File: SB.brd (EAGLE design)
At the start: 78 x 34 mm, 48 parts, among them IC1 ATMEGA32U4NT-TQFP, IC2 HX711-SOP16L, J2 RJ12, J3 AUDIO-JACK-PJ321, J4 NO/NC, J5 USB-C-16P-16P, K1 HE721C-DIP, Q1 2N7002, Q2 2N7002, Q3 2N3906

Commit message: Routing for v2.0 release
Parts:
- removed J4: NO/NC, SuperHouse-Connectors:1X03-P
- added SW1: SWITCH-SPDT-4TABSSMT, SuperHouse-Switches:MK-12C02
- L1: device SuperHouse-DiscreteSemi:0603 -> SuperHouse-DiscreteSemi:L0603
- MOD1: value OLED-I2C-128X32-0.91 -> OLED-I2C-128X32-0.91-HEADER; device SuperHouse-Displays:OLED-128X32-0.91 -> SuperHouse-Displays:OLED-128X32-0.91-HEADER
- moved C9 48.3 mm to (18.0, 3.50)
- moved R10 48.3 mm to (15.0, 2.50)
- moved R9 48.3 mm to (15.0, 4.50)
- moved R13 47.5 mm to (19.0, 8.50)
- moved IC2 47.2 mm to (29.0, 6.00)
- moved C8 46.7 mm to (23.0, 5.50)
- moved Q3 46.6 mm to (22.0, 11.0)
- moved C10 45.6 mm to (17.0, 10.5)
- moved R14 45.3 mm to (21.0, 7.00)
- moved C12 43.2 mm to (29.0, 12.0)
- moved C11 41.2 mm to (17.0, 14.5), turned to 90 degrees
- moved L1 38.5 mm to (19.0, 12.5), turned to 270 degrees
- moved R7 10.3 mm to (71.5, 16.0)
- moved C1 5.10 mm to (38.0, 17.0)
- moved C2 5.10 mm to (38.0, 14.5)
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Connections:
- net A+: now also J2.3; no longer J2.4
- net A-: now also J2.4; no longer J2.3
- net GND: now also SW1.MNT@1, SW1.MNT@2, SW1.MNT@3, SW1.MNT@4
- net N$4: now also K1.14, SW1.3; no longer J4.3, K1.1
- net N$6: now also K1.1, SW1.1; no longer J4.1, K1.14
- net N$9: now also SW1.2; no longer J4.2
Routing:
- net N$4: track 7.05 -> 57.6 mm
- net N$9: track 41.8 -> 10.4 mm
- net N$2: track 2.12 -> 28.6 mm, vias 0 -> 1
- net N$6: track 12.4 -> 34.8 mm
- net A+: track 0.00 -> 17.3 mm
- net E+: track 0.00 -> 17.3 mm
- net 5V: track 71.3 -> 86.4 mm, vias 5 -> 6
- net RESET: track 21.5 -> 35.6 mm
- net N$14: track 0.00 -> 11.2 mm
- net N$15: track 0.00 -> 11.1 mm
- net N$16: track 0.00 -> 10.9 mm
- net A-: track 0.00 -> 8.47 mm
- net D4_A6: track 45.6 -> 37.3 mm, vias 1 -> 2
- net N$21: track 0.00 -> 7.77 mm
- net N$20: track 0.00 -> 5.18 mm
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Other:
- board text added: "A+"
- board text added: "A-"
- board text added: "E+"
- board text added: "E-"
- board text added: "H+"
- board text added: "H-"

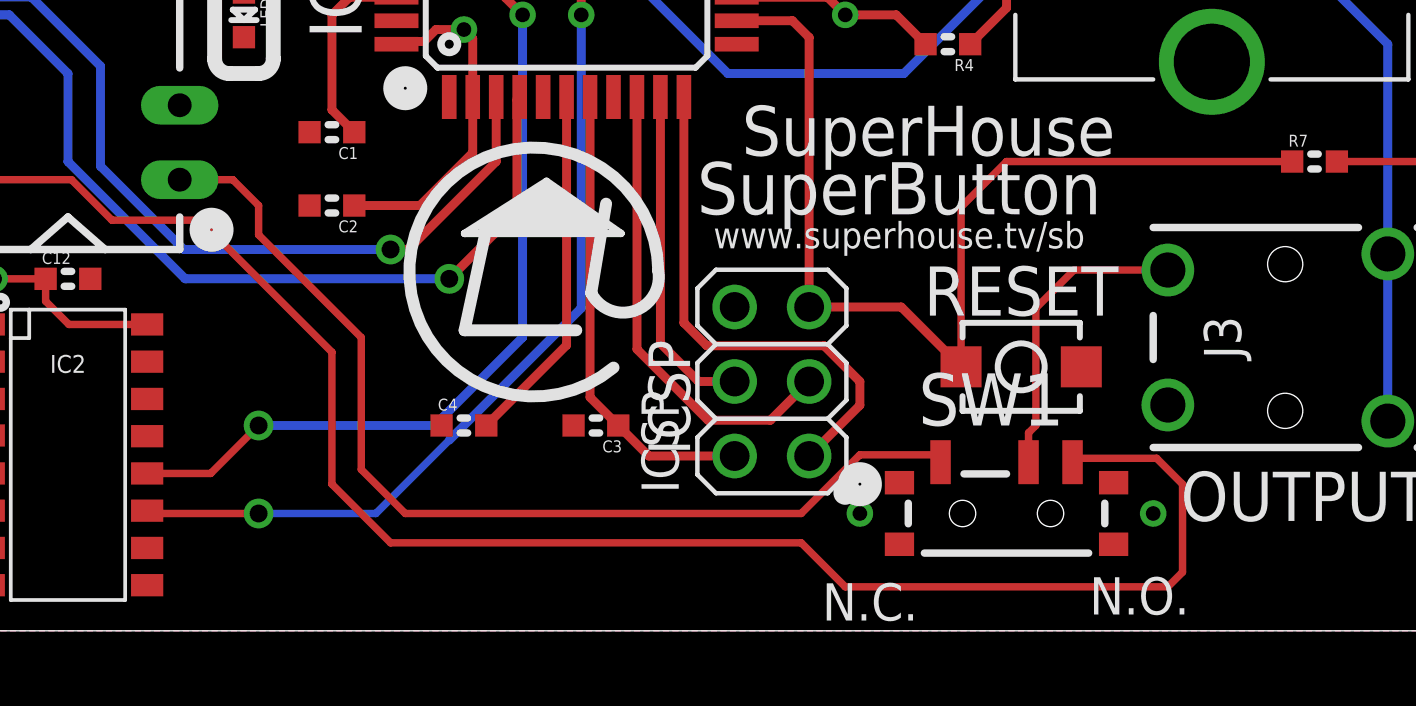
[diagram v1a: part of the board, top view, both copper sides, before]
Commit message: Synch with Fusion 360
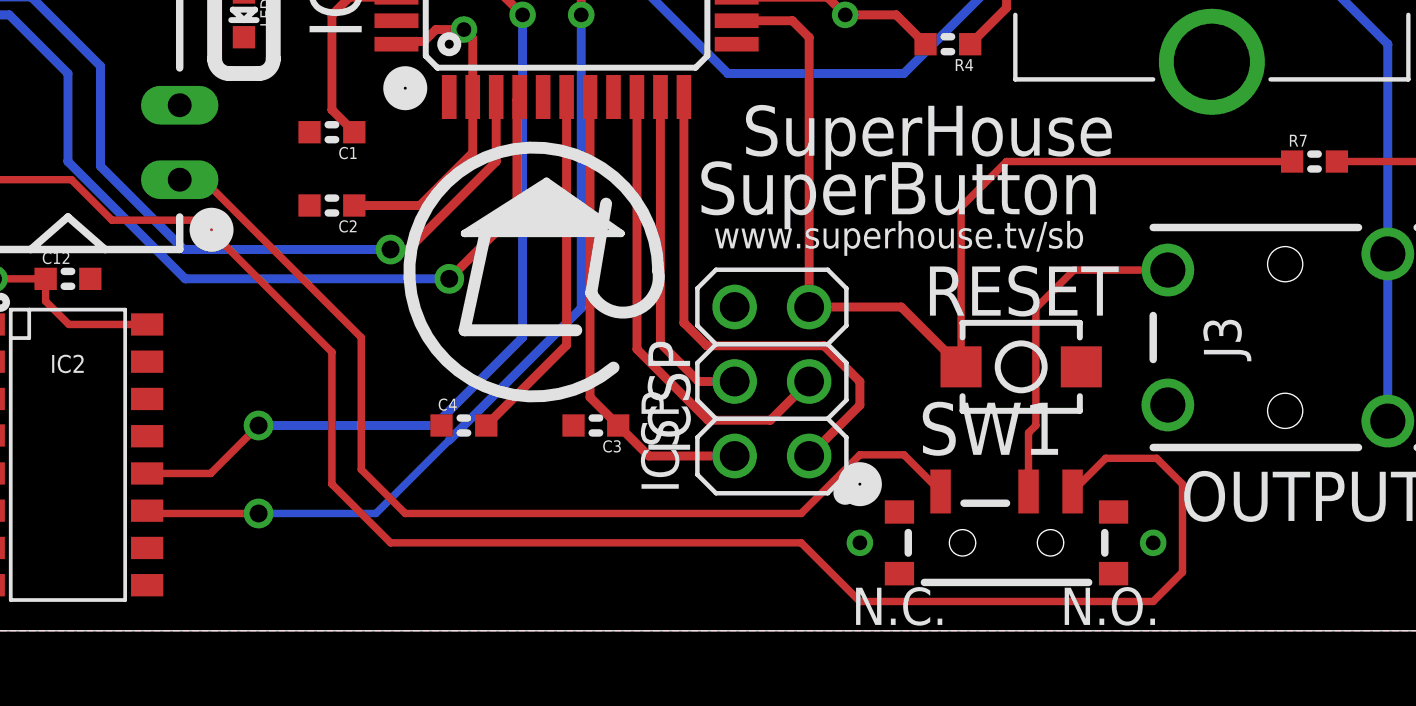
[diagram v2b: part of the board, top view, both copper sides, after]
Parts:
- R5, R6: value 4K7 -> 5k1
- moved SW1 1.00 mm to (61.0, 3.00)
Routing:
- net N$9: track 10.4 -> 11.4 mm
- net N$4: track 57.6 -> 58.4 mm
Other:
- board text added: "(C)2020 SuperHouse Automation P/L"
- board text removed: "(C)2019 SuperHouse Automation P/L"

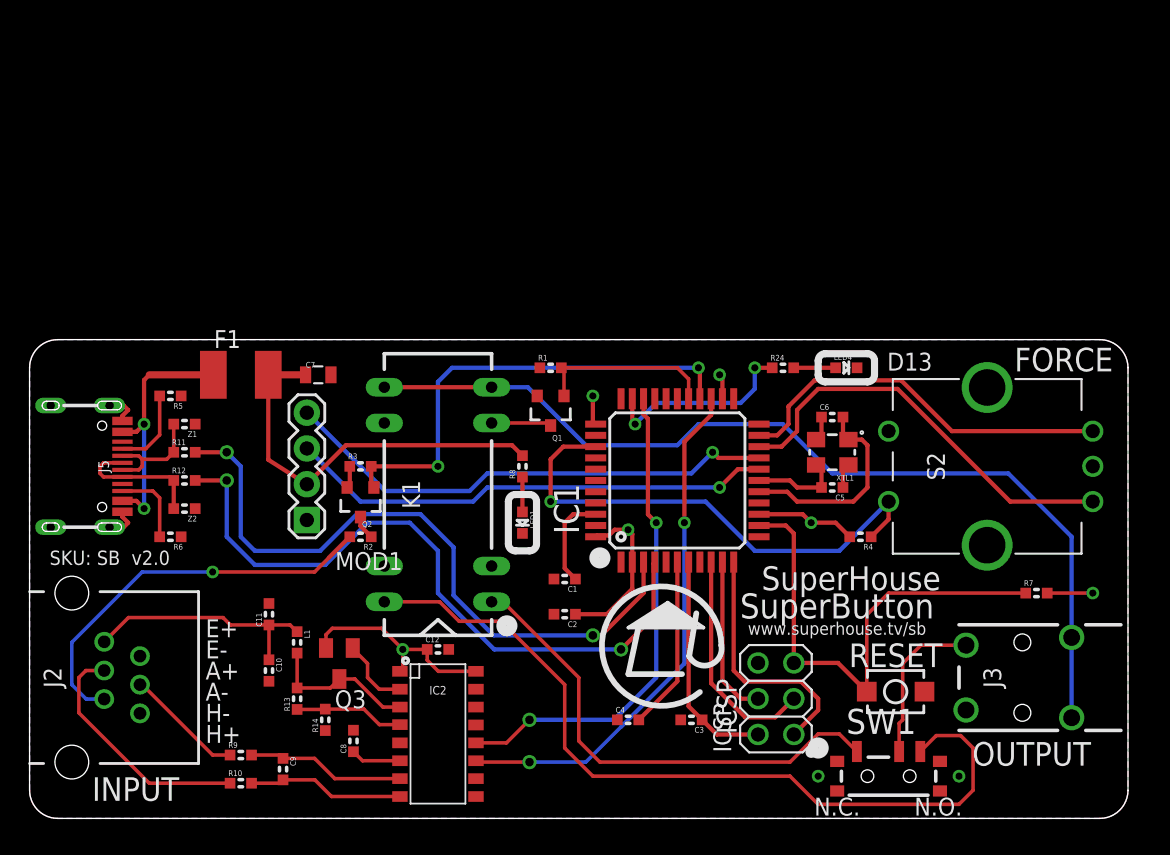
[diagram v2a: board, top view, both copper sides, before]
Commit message: Added mounting holes for v2.1 release
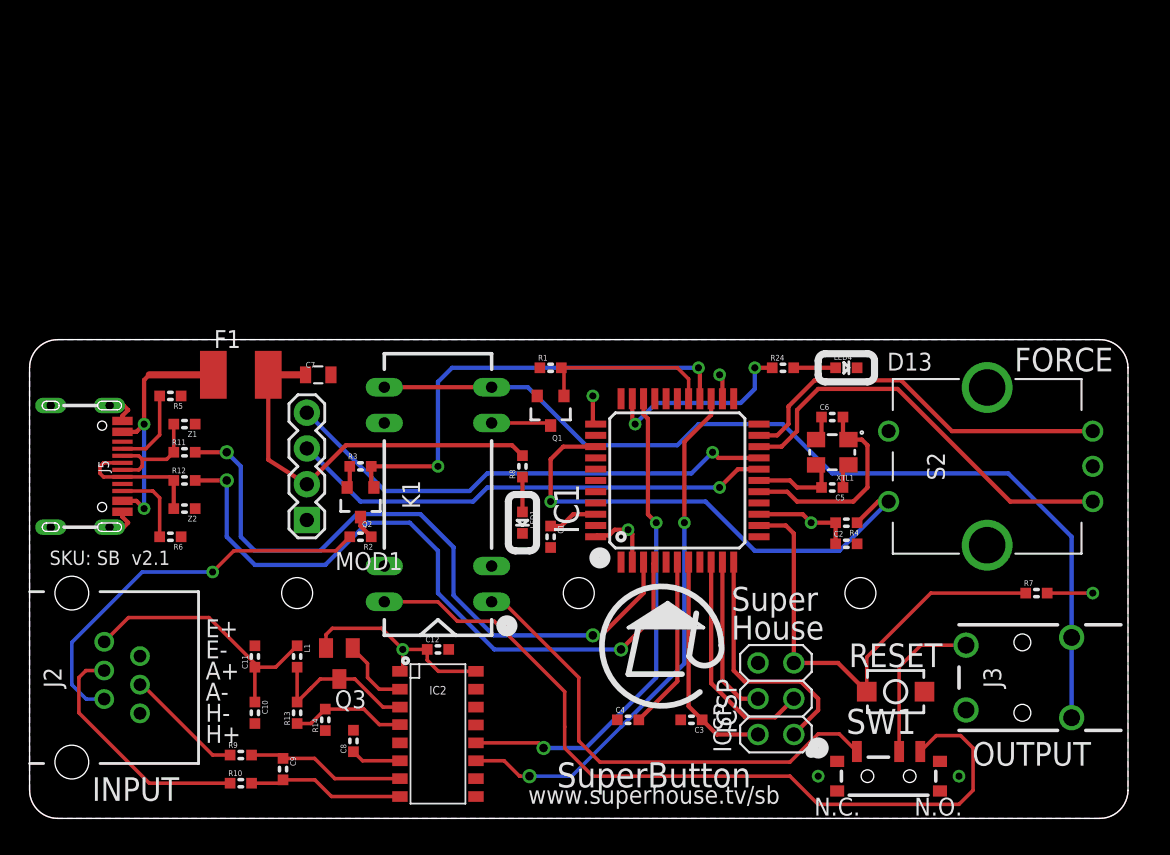
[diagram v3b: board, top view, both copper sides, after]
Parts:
- moved C2 20.6 mm to (58.0, 19.5), turned to 0 degrees
- moved C1 3.16 mm to (37.0, 20.0), turned to 270 degrees
- moved C10 3.16 mm to (16.0, 7.50)
- moved C11 3.16 mm to (16.0, 11.5)
- moved R4 1.41 mm to (58.0, 21.0)
- moved L1 1.00 mm to (19.0, 11.5)
- moved R13 1.00 mm to (19.0, 7.50)
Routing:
- net 5V: track 86.4 -> 79.8 mm
- net AREF: track 6.76 -> 3.55 mm
- net E+: track 17.3 -> 19.1 mm
- net RESET: track 35.6 -> 33.8 mm
- net D4_A6: track 37.3 -> 38.2 mm
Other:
- board text added: "SKU: SB v2.1"
- board text added: "Super House"
- board text removed: "SKU: SB v2.0"
- board text removed: "SuperHouse"

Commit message: Added Tare button and beep stretch switch, still for v2.1 release
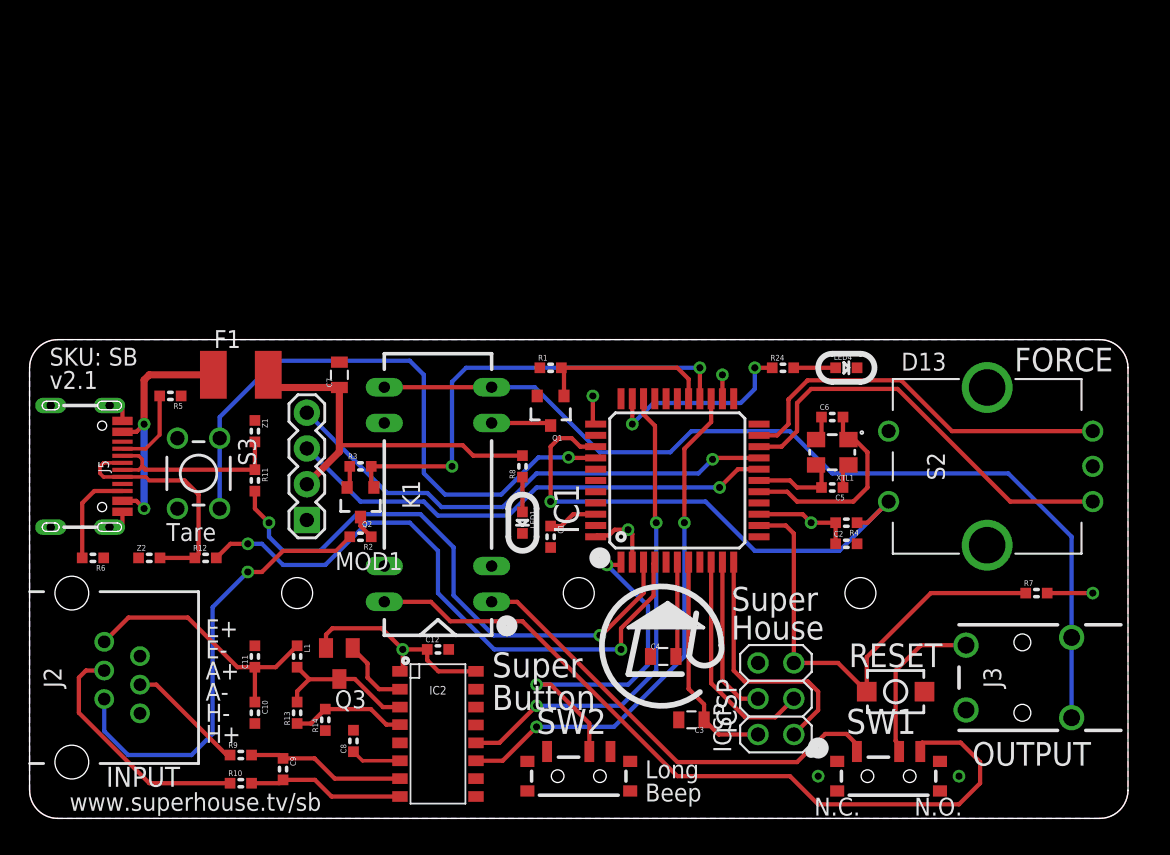
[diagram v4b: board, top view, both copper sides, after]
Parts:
- added S3: (no value), SuperHouse-Switches:TACTILE-PTH-4.5MM
- added SW2: SWITCH-SPDT-4TABSSMT, SuperHouse-Switches:MK-12C02
- C3, C4: device SuperHouse-DiscreteSemi:C0603 -> SuperHouse-DiscreteSemi:C0805
- moved R12 5.70 mm to (12.5, 18.5)
- moved R6 5.70 mm to (4.50, 18.5)
- moved R11 5.39 mm to (16.0, 24.0), turned to 270 degrees
- moved C4 5.15 mm to (45.0, 11.5)
- moved Z1 5.02 mm to (16.0, 27.5), turned to 270 degrees
- moved Z2 4.30 mm to (8.50, 18.5), turned to 0 degrees
- moved C7 1.50 mm to (22.0, 31.5), turned to 90 degrees
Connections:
- net A1: now also S3.1, S3.2
- net D7_AIN0: now also SW2.2
- net GND: now also S3.3, S3.4, SW2.3, SW2.MNT@1, SW2.MNT@2, SW2.MNT@3, SW2.MNT@4
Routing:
- net A1: track 0.00 -> 44.0 mm, vias 0 -> 1
- net D7_AIN0: track 0.00 -> 24.8 mm, vias 0 -> 2
- net D+: track 9.64 -> 16.9 mm
- net RD-: track 47.8 -> 40.8 mm
- net D-: track 7.96 -> 13.6 mm
- net 3V3: track 12.3 -> 6.72 mm
- net RD+: track 49.0 -> 43.7 mm
- net N$2: track 28.6 -> 32.1 mm
- net N$6: track 34.6 -> 32.3 mm
- net N$4: track 58.1 -> 55.8 mm
- net N$10: track 5.61 -> 7.10 mm
- net D4_A6: track 38.2 -> 37.0 mm
- net 5V: track 79.8 -> 78.7 mm
- net A0: track 36.3 -> 37.4 mm
- net D3_SCL: track 34.6 -> 35.5 mm
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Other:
- board text added: "Long Beep"
- board text added: "Super Button"
- board text added: "Tare"
- board text removed: "SuperButton"

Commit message: Removed haptic feedback and changed to RJ10 connector for v3.0 release
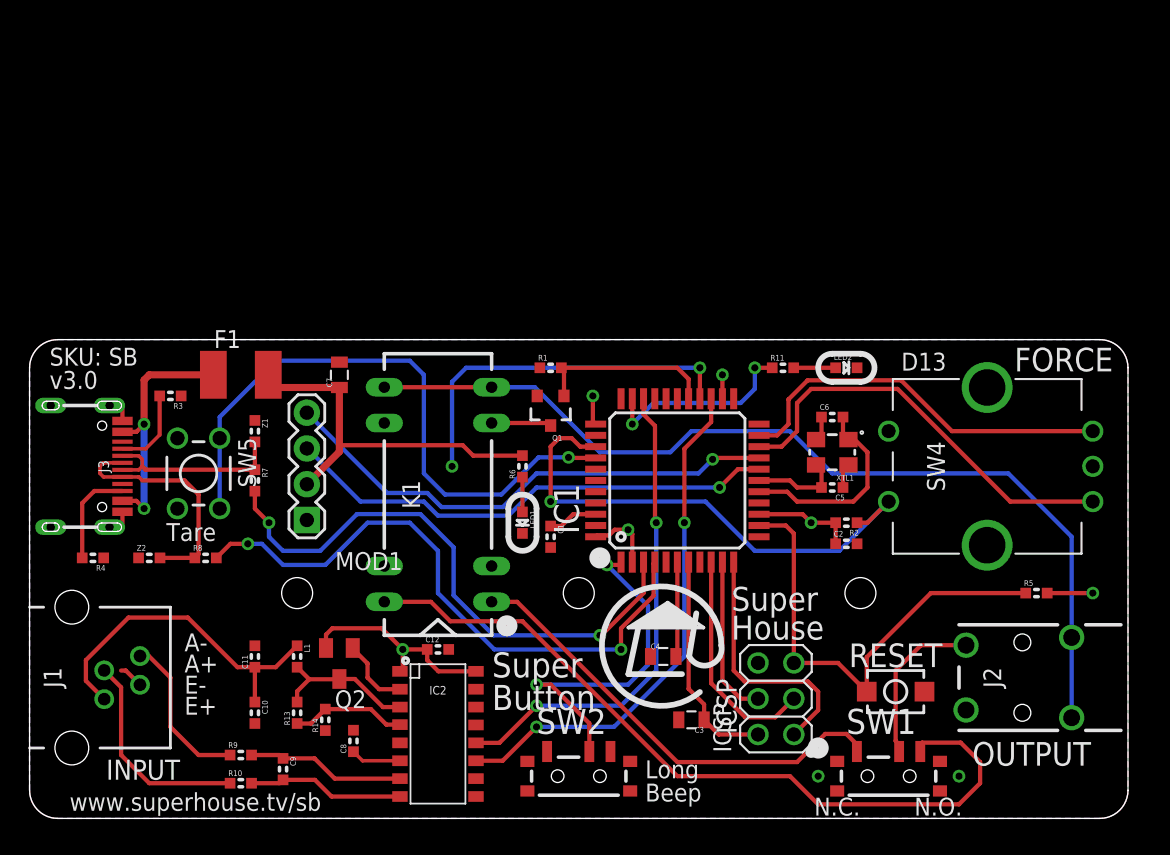
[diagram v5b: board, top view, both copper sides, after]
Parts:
- removed J5: USB-C-16P-16P, SuperHouse-Connectors:USB-C-16P
- removed Q3: 2N3906, SuperHouse-DiscreteSemi:SOT23-BEC
- removed R12: 22R, SuperHouse-DiscreteSemi:R0603
- removed R24: 1K, SuperHouse-DiscreteSemi:R0603
- added J1: RJ10-WURTH, SuperHouse-Connectors:RJ10
- J2: value RJ12 -> AUDIO-JACK-PJ321; device SuperHouse-Connectors:RJ12 -> SuperHouse-Connectors:AUDIO-JACK-PJ321
- J3: value AUDIO-JACK-PJ321 -> USB-C-16P-16P; device SuperHouse-Connectors:AUDIO-JACK-PJ321 -> SuperHouse-Connectors:USB-C-16P
- Q2: value 2N7002 -> 2N3906; device SuperHouse-DiscreteSemi:SOT23-3 -> SuperHouse-DiscreteSemi:SOT23-BEC
- R11: value 22R -> 1K
- R2: value 150R -> 10K
- R3, R4: value 10K -> 5k1
- R5: value 5k1 -> 10K
- R6: value 5k1 -> 4K7
- R7: value 10K -> 22R
- R8: value 4K7 -> 22R
- moved J3 74.0 mm to (1.50, 25.0), turned to 270 degrees
- moved J2 71.0 mm to (74.0, 10.0), turned to 90 degrees
- moved R5 63.1 mm to (71.5, 16.0), turned to 0 degrees
- moved R7 56.1 mm to (16.0, 24.0), turned to 270 degrees
- moved R4 53.6 mm to (4.50, 18.5)
- moved R11 38.3 mm to (53.5, 32.0), turned to 0 degrees
- moved R2 34.5 mm to (58.0, 21.0)
- moved R6 31.2 mm to (35.0, 25.0), turned to 90 degrees
- moved R8 23.4 mm to (12.5, 18.5), turned to 0 degrees
- moved R3 14.4 mm to (10.0, 30.0), turned to 180 degrees
- moved Q2 11.6 mm to (22.0, 11.0)
- renumbered LED4 to LED2, S1 to SW3, S2 to SW4, S3 to SW5
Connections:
- removed net N$2: J2.5, R2.2
- removed net N$8: Q2.3, R2.1
- net 5V: now also Q2.E, R2.2, R5.2, R6.2; no longer J2.6, Q3.E, R4.2, R7.2, R8.2
- net A+: now also J1.P$3; no longer J2.3
- net A-: now also J1.P$4; no longer J2.4
- net A0: now also R2.1; no longer R4.1
- net D+: now also J3.A6, J3.B6, R8.1; no longer J5.A6, J5.B6, R12.1
- net D-: now also J3.A7, J3.B7, R7.1; no longer J5.A7, J5.B7, R11.1
- net D12: no longer Q2.1, R3.2
- net D13: now also R11.1; no longer R24.1
- net E+: now also J1.P$1; no longer J2.1
- net GND: now also J1.P$2, J3.A12B1, J3.A1B12, J3.FIX1, J3.FIX2, J3.FIX3, J3.FIX4, R4.1; no longer J2.2, J5.A12B1, J5.A1B12, J5.FIX1, J5.FIX2, J5.FIX3, J5.FIX4, Q2.2, R5.1, R6.1
- net N$1: now also R11.2; no longer R24.2
- net N$10: now also J3.B5, R4.2; no longer J5.B5, R6.2
- net N$13: now also J3.A5, R3.2; no longer J5.A5, R5.2
- net N$16: now also Q2.C; no longer Q3.C
- net N$20: now also Q2.B; no longer Q3.B
- net N$5: now also R6.1; no longer R8.1
- net N$7: now also J2.4A, J2.4B; no longer J3.4A, J3.4B
- net N$9: now also J2.3; no longer J3.3
- net RD+: now also R8.2; no longer R12.2
- net RD-: now also R7.2; no longer R11.2
- net RESET: now also R5.1; no longer R7.1
- net USB+: now also J3.A4B9, J3.A9B4; no longer J5.A4B9, J5.A9B4
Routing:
- net N$2: track 32.1 -> 0.00 mm, vias 1 -> 0
- net D12: track 33.7 -> 26.2 mm
- net E+: track 19.0 -> 24.1 mm
- net A-: track 8.47 -> 11.4 mm
- net A+: track 17.3 -> 15.1 mm
- net N$8: track 1.72 -> 0.00 mm
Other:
- board text added: "SKU: SB v3.0"
- board text removed: "H+"
- board text removed: "H-"
- board text removed: "SKU: SB v2.1"
